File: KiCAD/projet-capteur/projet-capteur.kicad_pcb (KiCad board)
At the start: 2 copper layers, 68.6 x 53.3 mm, 9 parts, among them J1 Power, J2 Digital/PWM, J3 Analog, J4 Digital/PWM

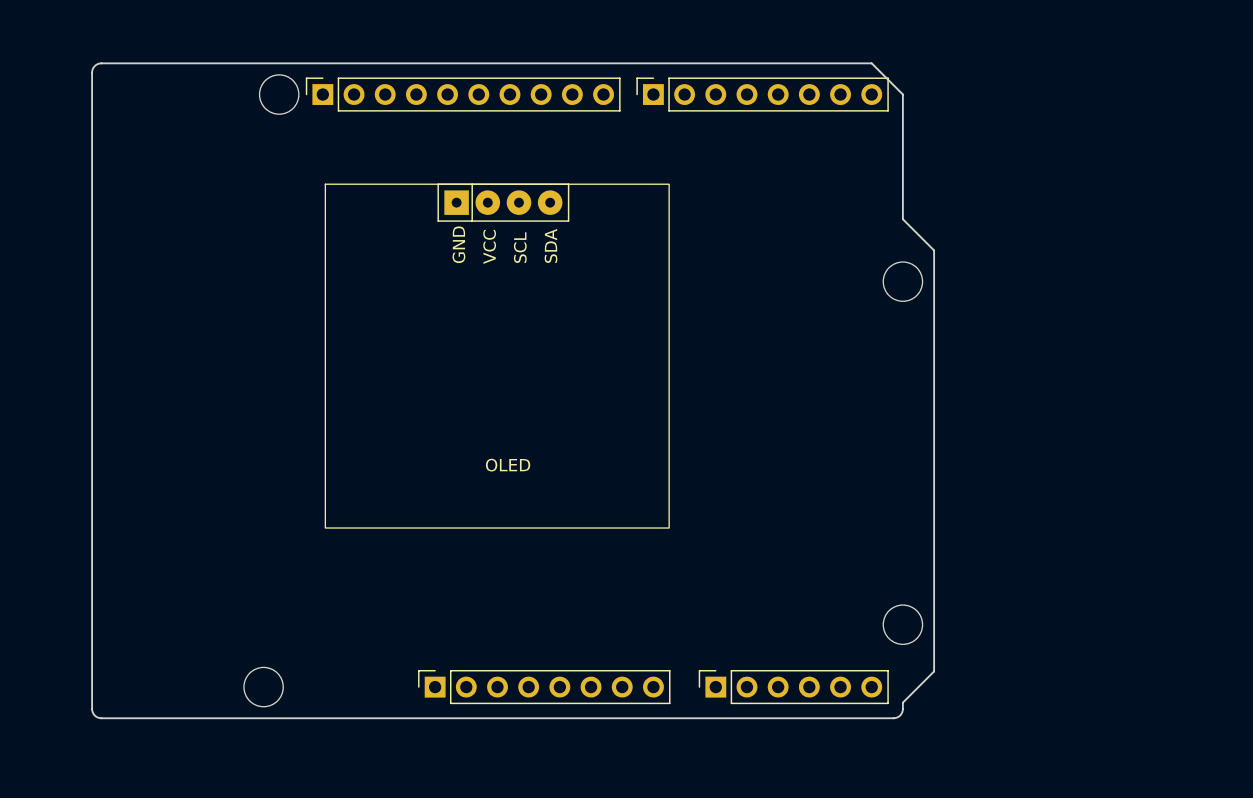
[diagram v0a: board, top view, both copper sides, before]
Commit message: Ajout ecran OLED + Schema
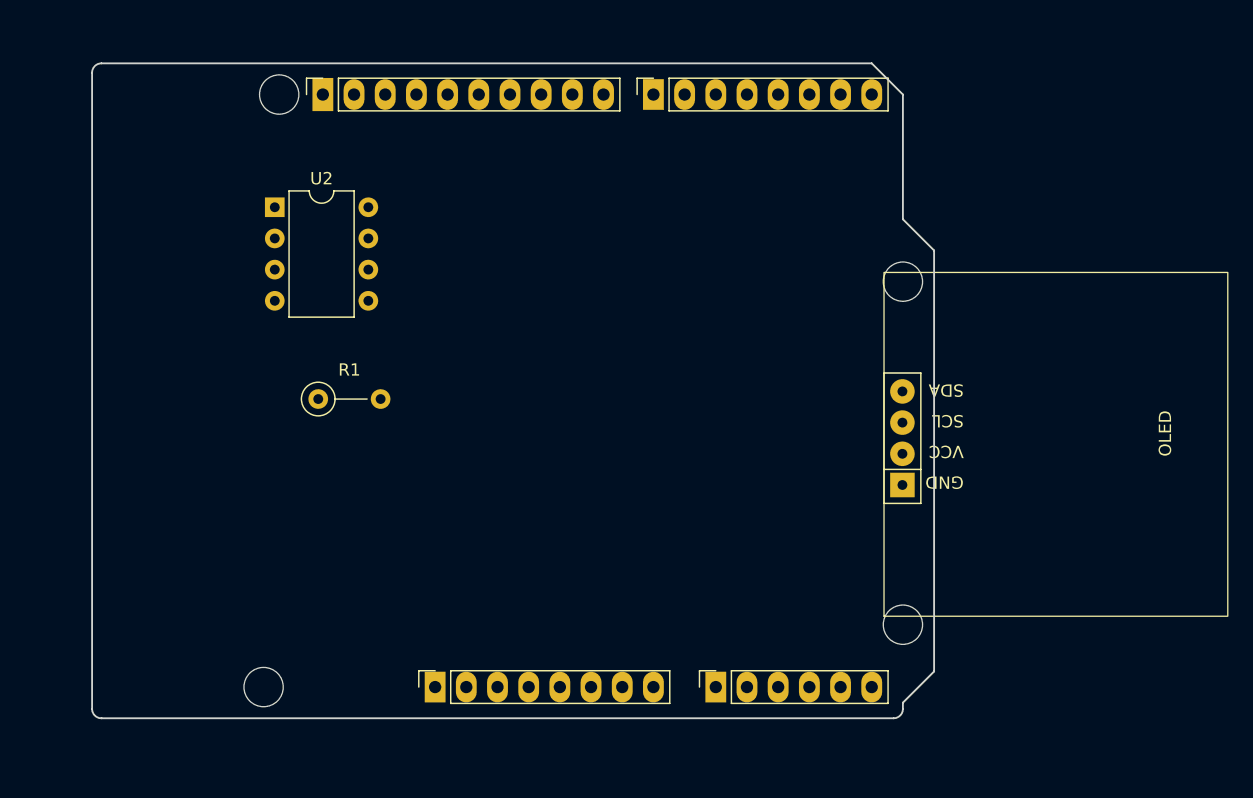
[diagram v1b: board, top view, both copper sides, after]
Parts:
- added R1: 100k, Resistor_THT:R_Axial_DIN0207_L6.3mm_D2.5mm_P5.08mm_Vertical, F.Cu at (118.4, 74.0)
- added U2: LTC1050, Package_DIP:DIP-8_W7.62mm, F.Cu at (114.9, 58.4)
- moved U1 37.7 mm to (166.0, 77.2), turned to 90 degrees

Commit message: Ajout du HC-05
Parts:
- added R1: 10k, Resistor_THT:R_Axial_DIN0207_L6.3mm_D2.5mm_P5.08mm_Vertical, F.Cu at (134.4, 74.0)
- added R3: 1k, Resistor_THT:R_Axial_DIN0207_L6.3mm_D2.5mm_P5.08mm_Vertical, F.Cu at (134.4, 65.8)
- added R4: 100k, Resistor_THT:R_Axial_DIN0207_L6.3mm_D2.5mm_P5.08mm_Vertical, F.Cu at (134.4, 69.9)
- added R5: 1k, Resistor_THT:R_Axial_DIN0207_L6.3mm_D2.5mm_P5.08mm_Vertical, F.Cu at (134.4, 78.0)
- added U3: ~, MyLibEmpreinte:HC-05, F.Cu at (113.5, 83.0)
- renumbered J3 to J2, J2 to J3, R1 to R2

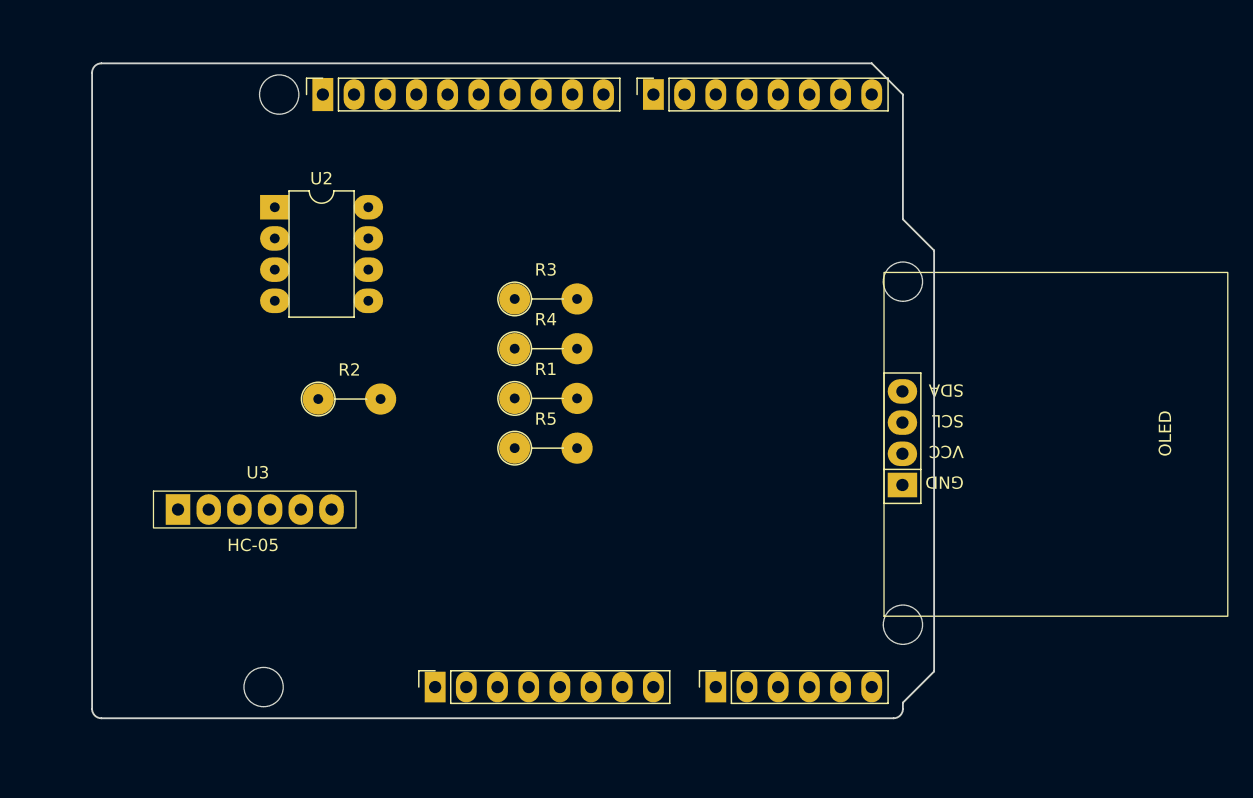
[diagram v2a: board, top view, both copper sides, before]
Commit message: rajout des condesateur sur le pcb
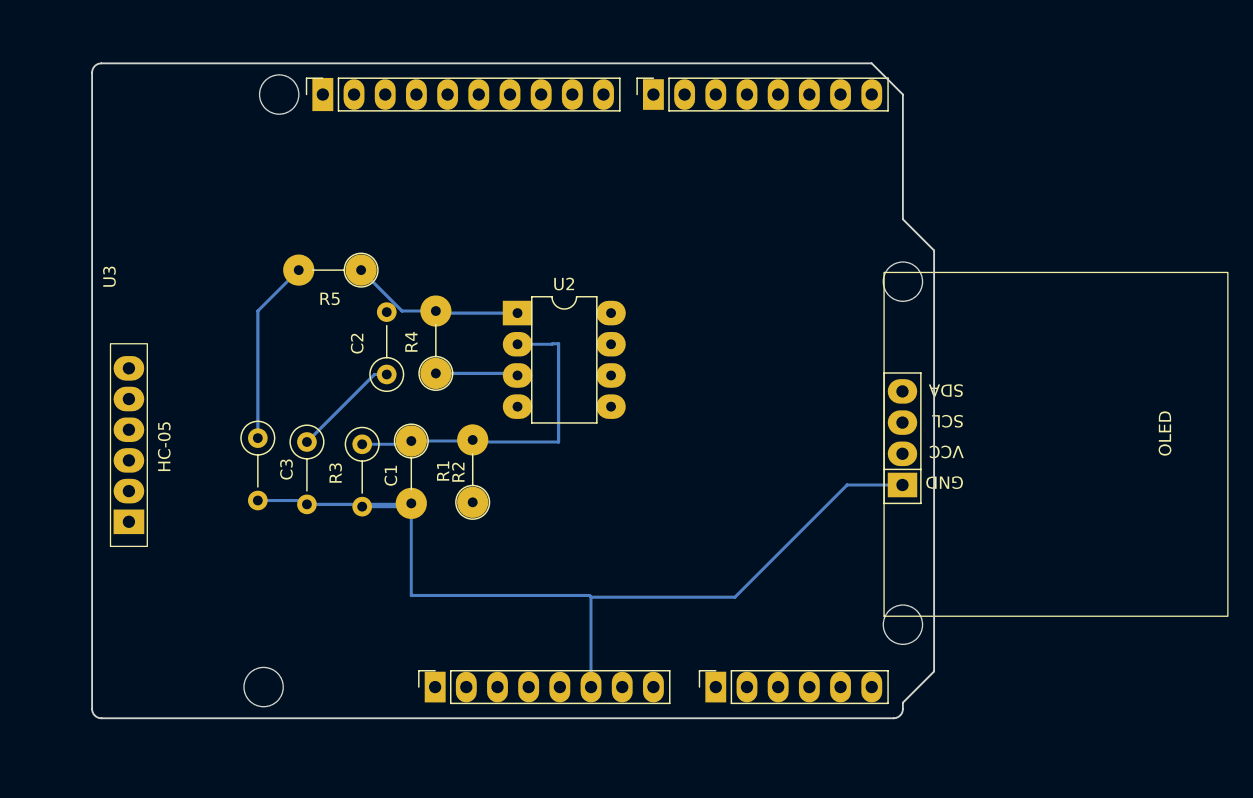
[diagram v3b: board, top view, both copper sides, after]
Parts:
- added C1: 100n, Resistor_THT:R_Axial_DIN0207_L6.3mm_D2.5mm_P5.08mm_Vertical, F.Cu at (122.0, 77.7)
- added C2: 1u, Resistor_THT:R_Axial_DIN0207_L6.3mm_D2.5mm_P5.08mm_Vertical, F.Cu at (124.0, 72.0)
- added C3: 100n, Resistor_THT:R_Axial_DIN0207_L6.3mm_D2.5mm_P5.08mm_Vertical, F.Cu at (113.5, 77.2)
- moved U2 21.6 mm to (134.7, 67.0)
- moved R3 20.5 mm to (117.5, 77.5), turned to -90 degrees
- moved R5 19.1 mm to (121.9, 63.5), turned to 180 degrees
- moved U3 11.9 mm to (103.0, 77.5), turned to 90 degrees
- moved R1 9.13 mm to (131.0, 82.4), turned to 90 degrees
- moved R2 8.32 mm to (126.0, 77.4), turned to -90 degrees
- moved R4 6.73 mm to (128.0, 71.9), turned to 90 degrees
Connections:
- J1 pad 5: +5V -> 5V
- U1 pad 1: unconnected-(U1-GND-Pad1) -> GND
- U1 pad 2: unconnected-(U1-VCC-Pad2) -> 5V
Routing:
- net GND: track 0.00 -> 75.0 mm
- net Net-(U2--): track 0.00 -> 27.6 mm
- net Net-(U2-+): track 0.00 -> 15.5 mm
- net ADC: track 0.00 -> 15.1 mm
- net Net-(C2-Pad2): track 0.00 -> 14.2 mm

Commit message: pin a jour pour le ltc1050 hc05 connecté
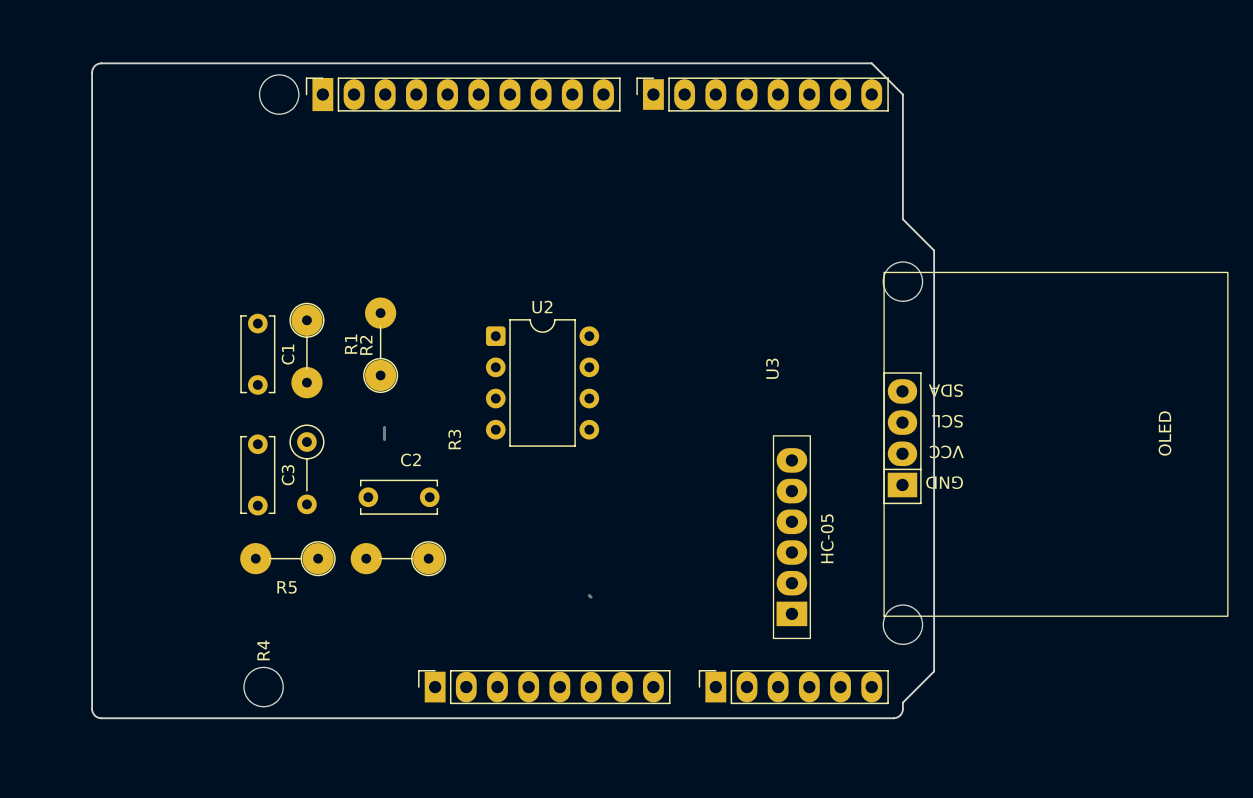
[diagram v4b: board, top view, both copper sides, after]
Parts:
- C1, C2, C3: footprint Resistor_THT:R_Axial_DIN0207_L6.3mm_D2.5mm_P5.08mm_Vertical -> Capacitor_THT:C_Disc_D6.0mm_W2.5mm_P5.00mm
- moved U3 54.5 mm to (157.0, 85.0)
- moved R5 23.8 mm to (118.4, 87.0)
- moved R4 15.1 mm to (127.4, 87.0), turned to 180 degrees
- moved C1 13.0 mm to (113.5, 67.9)
- moved R2 13.0 mm to (117.5, 67.6)
- moved R1 12.8 mm to (123.5, 72.1)
- moved C2 10.1 mm to (122.5, 82.0), turned to 0 degrees
- moved U2 2.58 mm to (132.9, 68.9)
- moved C3 0.50 mm to (113.5, 77.7)
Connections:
- J2 pad 5: /SDA/A4 -> SDA
- J2 pad 6: /SCL/A5 -> SCL
- J3 pad 1: /SCL/A5 -> SCL
- J3 pad 2: /SDA/A4 -> SDA
- U1 pad 3: unconnected-(U1-SCL-Pad3) -> SCL
- U1 pad 4: unconnected-(U1-SDA-Pad4) -> SDA
- U2 pad 1: Net-(C2-Pad2) -> (no net)
- U2 pad 4: (no net) -> GND
- U2 pad 6: (no net) -> Net-(C2-Pad2)
- U2 pad 7: (no net) -> 5V
- U3 pad 2: unconnected-(U3-Vcc(+5V)-Pad2) -> 5V
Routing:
- net GND: track 75.0 -> 1.89 mm
- net Net-(U2--): track 27.6 -> 0.74 mm
- net ADC: track 15.1 -> 0.00 mm
- net Net-(U2-+): track 15.5 -> 1.00 mm
- net Net-(C2-Pad2): track 14.2 -> 0.24 mm

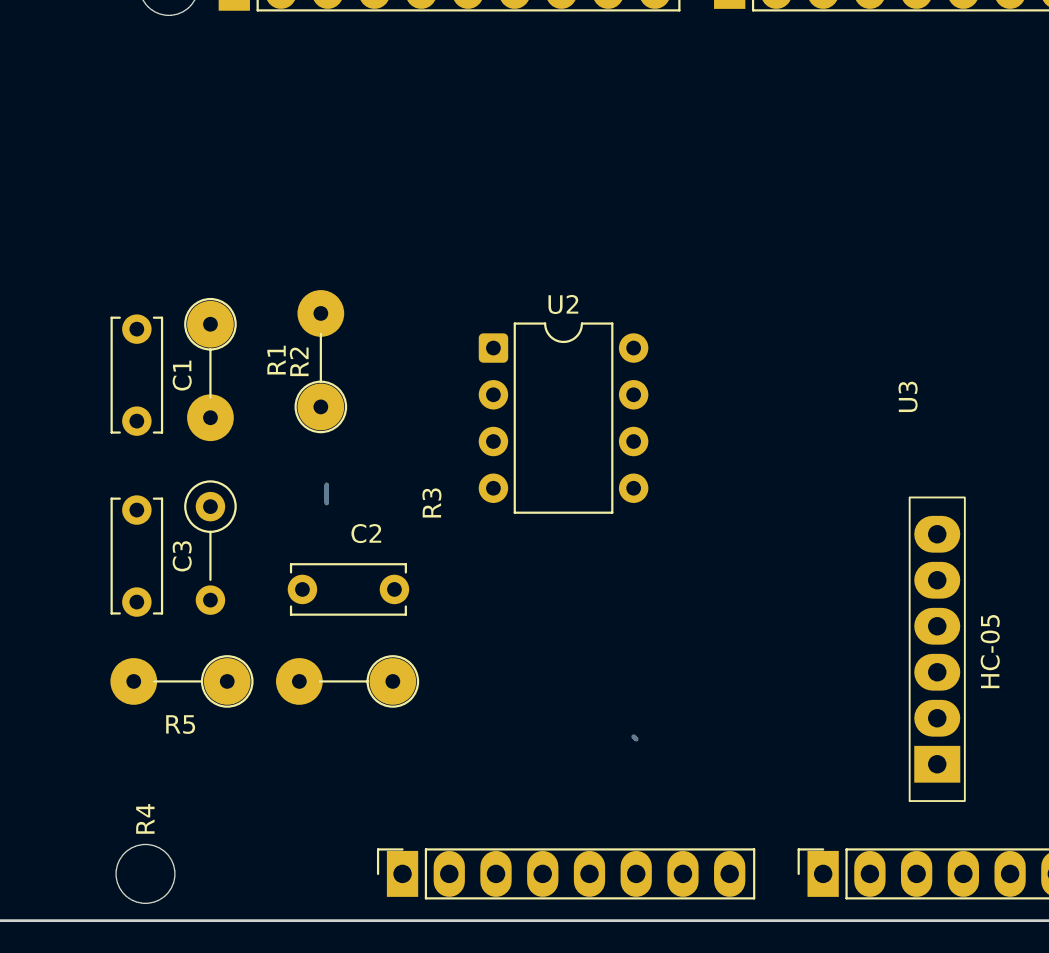
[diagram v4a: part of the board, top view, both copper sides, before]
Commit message: Ajout du Flex Sensor et DPotentiometre
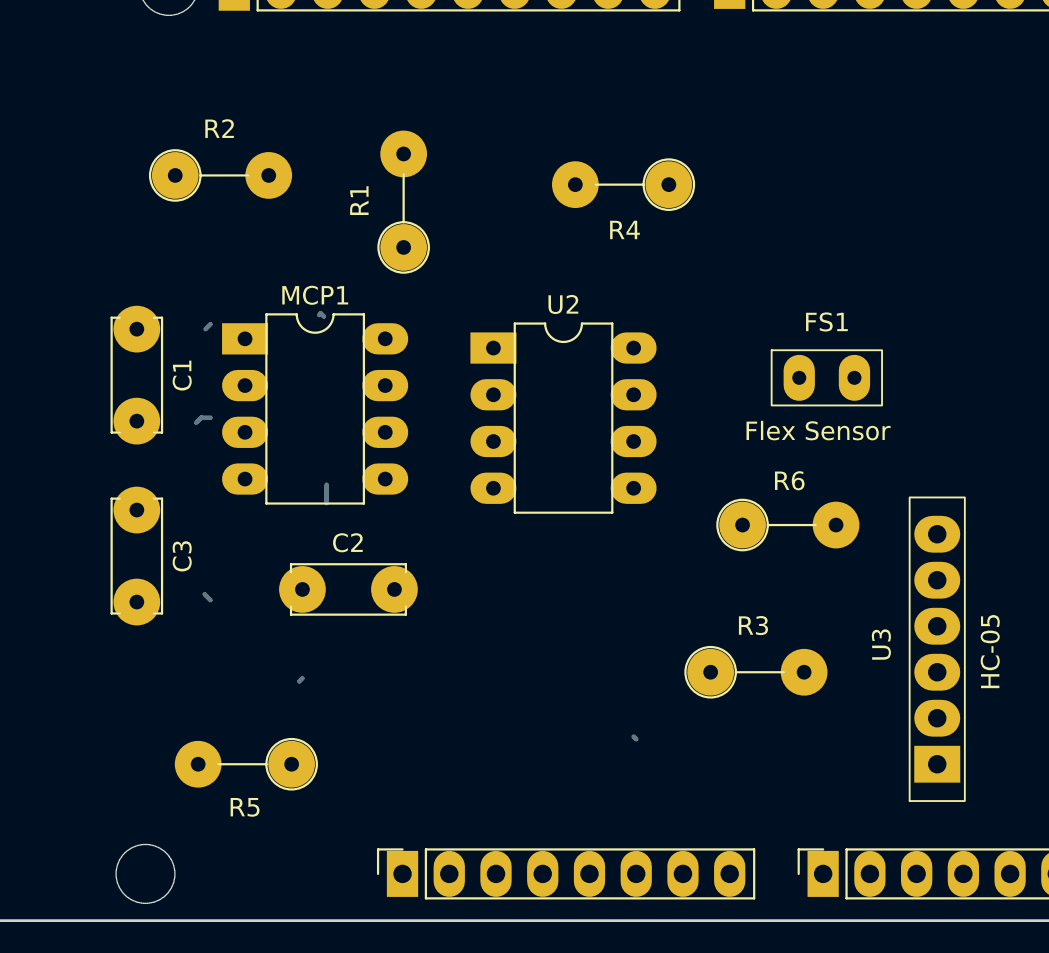
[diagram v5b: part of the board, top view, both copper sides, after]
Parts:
- added FS1: ~, MyLibEmpreinte:Flex Sensor, F.Cu at (151.0, 70.5)
- added MCP1: ~, Package_DIP:DIP-8_W7.62mm, F.Cu at (119.4, 68.4)
- added R6: R, Resistor_THT:R_Axial_DIN0207_L6.3mm_D2.5mm_P5.08mm_Vertical, F.Cu at (146.4, 78.5)
- moved R4 30.9 mm to (142.4, 60.0)
- moved R3 28.6 mm to (144.7, 86.5), turned to 0 degrees
- moved R1 9.77 mm to (128.0, 63.4)
- moved R2 8.31 mm to (115.6, 59.5), turned to 0 degrees
- moved R5 5.70 mm to (121.9, 91.5)
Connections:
- C3 pad 1: ADC -> Output Capteur
- J2 pad 1: /A0 -> Output Capteur
- R5 pad 2: ADC -> Output Capteur
